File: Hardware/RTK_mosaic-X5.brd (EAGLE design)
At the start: 151.8 x 101.6 mm, 370 parts, among them J2 MAGJACK-POE, J3 MICRO-SD-PUSH-PUSH-EXT-PIN, J4 Vertical Qwiic Connector, J9 MAGJACK-POE, U1 ESP32-WROVER-IE, U10 POE_PSU-DP990X, U11 SN74AVC4T774PW, U17 URB2405YMD, U2 CH340C, U3 AP7361C-33FGEUDFN-8, U4 TXS0108, U5 TXS0108, U6 AP7361C-33FGEUDFN-8, U7 KSZ8041NL, U8 MOSAIC-X5X5, U9 KSZ8041NL

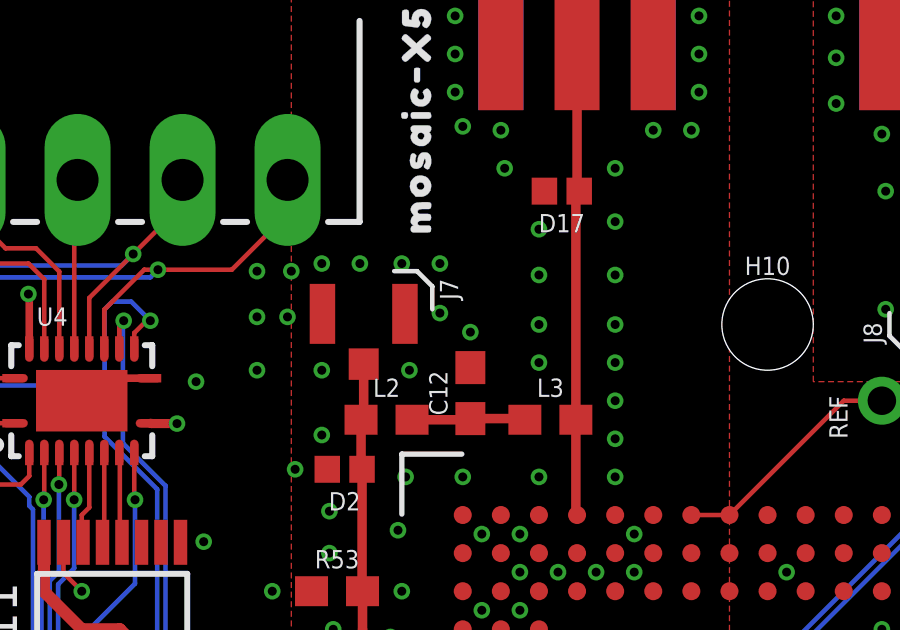
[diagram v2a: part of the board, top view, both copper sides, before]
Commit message: Adding u.FL connector for mosaic-H - with standoff holes for a u.FL-SMA daughter board
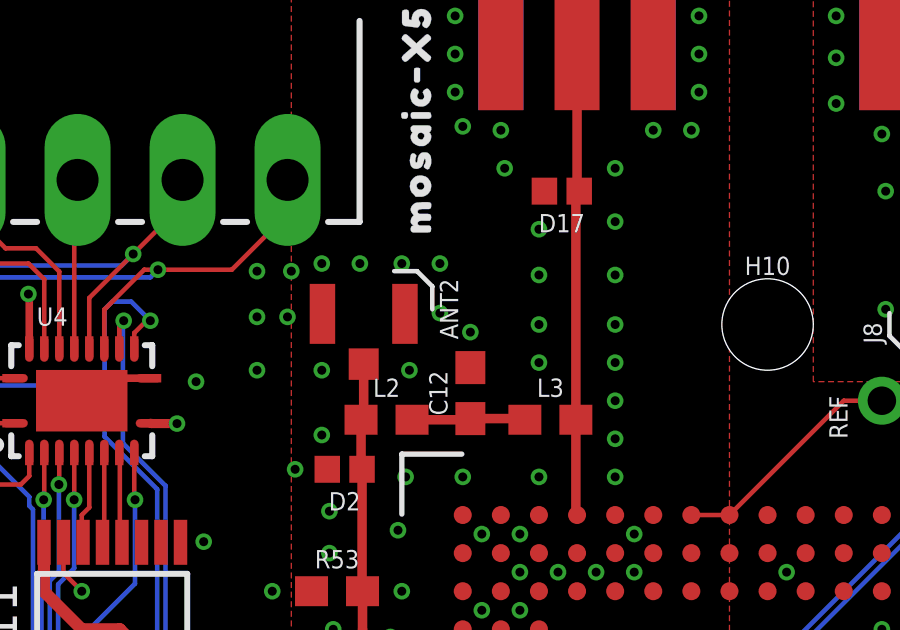
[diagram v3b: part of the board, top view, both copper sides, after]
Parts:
- removed J7: (no value), SparkFun-Connectors:U.FL_REDUCED_FOOTPRINT
- added ANT2: DNP, SparkFun-Connectors:U.FL_REDUCED_FOOTPRINT__NO_CREAM
- renumbered MOSAIC_RF to ANT1
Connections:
- net N$6 renamed VANT
- net ANT2: now also ANT2.FEED; no longer J7.FEED
- net GND: now also ANT2.1, ANT2.2; no longer J7.1, J7.2
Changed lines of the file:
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@@
 <drawing>
 <settings>
-<setting alwaysvectorfont="no"/>
+<setting alwaysvectorfont="yes"/>
 <setting verticaltext="up"/>
 </settings>
@@
 <layers>
 <layer number="1" name="Top" color="4" fill="1" visible="yes" active="yes"/>
-<layer number="2" name="Route2" color="63" fill="1" visible="yes" active="yes"/>
-<layer number="15" name="Route15" color="23" fill="1" visible="yes" active="yes"/>
+<layer number="2" name="Route2" color="63" fill="1" visible="no" active="yes"/>
+<layer number="15" name="Route15" color="23" fill="1" visible="no" active="yes"/>
 <layer number="16" name="Bottom" color="1" fill="1" visible="yes" active="yes"/>
 <layer number="17" name="Pads" color="2" fill="1" visible="yes" active="yes"/>
@@
 <layer number="23" name="tOrigins" color="15" fill="1" visible="yes" active="yes"/>
 <layer number="24" name="bOrigins" color="15" fill="1" visible="yes" active="yes"/>
-<layer number="25" name="tNames" color="7" fill="1" visible="yes" active="yes"/>
-<layer number="26" name="bNames" color="7" fill="1" visible="yes" active="yes"/>
-<layer number="27" name="tValues" color="7" fill="1" visible="yes" active="yes"/>
-<layer number="28" name="bValues" color="7" fill="1" visible="yes" active="yes"/>
-<layer number="29" name="tStop" color="7" fill="3" visible="yes" active="yes"/>
-<layer number="30" name="bStop" color="7" fill="6" visible="yes" active="yes"/>
-<layer number="31" name="tCream" color="7" fill="4" visible="yes" active="yes"/>
-<layer number="32" name="bCream" color="7" fill="5" visible="yes" active="yes"/>
-<layer number="33" name="tFinish" color="6" fill="3" visible="yes" active="yes"/>
-<layer number="34" name="bFinish" color="6" fill="6" visible="yes" active="yes"/>
-<layer number="35" name="tGlue" color="7" fill="4" visible="yes" active="yes"/>
-<layer number="36" name="bGlue" color="7" fill="5" visible="yes" active="yes"/>
-<layer number="37" name="tTest" color="7" fill="1" visible="yes" active="yes"/>
-<layer number="38" name="bTest" color="7" fill="1" visible="yes" active="yes"/>
-<layer number="39" name="tKeepout" color="4" fill="11" visible="yes" active="yes"/>
-<layer number="40" name="bKeepout" color="1" fill="11" visible="yes" active="yes"/>
-<layer number="41" name="tRestrict" color="4" fill="10" visible="yes" active="yes"/>
-<layer number="42" name="bRestrict" color="1" fill="10" visible="yes" active="yes"/>
-<layer number="43" name="vRestrict" color="2" fill="10" visible="yes" active="yes"/>
-<layer number="44" name="Drills" color="7" fill="1" visible="yes" active="yes"/>
+<layer number="25" name="tNames" color="7" fill="1" visible="no" active="yes"/>
+<layer number="26" name="bNames" color="7" fill="1" visible="no" active="yes"/>
+<layer number="27" name="tValues" color="7" fill="1" visible="no" active="yes"/>
+<layer number="28" name="bValues" color="7" fill="1" visible="no" active="yes"/>
+<layer number="29" name="tStop" color="7" fill="3" visible="no" active="yes"/>
+<layer number="30" name="bStop" color="7" fill="6" visible="no" active="yes"/>
+<layer number="31" name="tCream" color="7" fill="4" visible="no" active="yes"/>
+<layer number="32" name="bCream" color="7" fill="5" visible="no" active="yes"/>
+<layer number="33" name="tFinish" color="6" fill="3" visible="no" active="yes"/>
+<layer number="34" name="bFinish" color="6" fill="6" visible="no" active="yes"/>
+<layer number="35" name="tGlue" color="7" fill="4" visible="no" active="yes"/>
+<layer number="36" name="bGlue" color="7" fill="5" visible="no" active="yes"/>
+<layer number="37" name="tTest" color="7" fill="1" visible="no" active="yes"/>
+<layer number="38" name="bTest" color="7" fill="1" visible="no" active="yes"/>
+<layer number="39" name="tKeepout" color="4" fill="11" visible="no" active="yes"/>
+<layer number="40" name="bKeepout" color="1" fill="11" visible="no" active="yes"/>
+<layer number="41" name="tRestrict" color="4" fill="10" visible="no" active="yes"/>
+<layer number="42" name="bRestrict" color="1" fill="10" visible="no" active="yes"/>
+<layer number="43" name="vRestrict" color="2" fill="10" visible="no" active="yes"/>
+<layer number="44" name="Drills" color="7" fill="1" visible="no" active="yes"/>
 <layer number="45" name="Holes" color="7" fill="1" visible="yes" active="yes"/>
-<layer number="46" name="Milling" color="3" fill="1" visible="yes" active="yes"/>
-<layer number="47" name="Measures" color="7" fill="1" visible="yes" active="yes"/>
-<layer number="48" name="Document" color="7" fill="1" visible="yes" active="yes"/>
-<layer number="49" name="Reference" color="7" fill="1" visible="yes" active="yes"/>
-<layer number="50" name="dxf" color="7" fill="1" visible="yes" active="yes"/>
+<layer number="46" name="Milling" color="3" fill="1" visible="no" active="yes"/>
+<layer number="47" name="Measures" color="7" fill="1" visible="no" active="yes"/>
+<layer number="48" name="Document" color="7" fill="1" visible="no" active="yes"/>
+<layer number="49" name="Reference" color="7" fill="1" visible="no" active="yes"/>
+<layer number="50" name="dxf" color="7" fill="1" visible="no" active="yes"/>
 <layer number="51" name="tDocu" color="6" fill="1" visible="yes" active="yes"/>
-<layer number="52" name="bDocu" color="7" fill="1" visible="yes" active="yes"/>
+<layer number="52" name="bDocu" color="7" fill="1" visible="no" active="yes"/>
 <layer number="3" name="Route3" color="17" fill="1" visible="no" active="no"/>
 <layer number="4" name="Route4" color="18" fill="1" visible="no" active="no"/>
@@
 <attribute name="VALUE" x="43.18" y="88.265" size="0.6096" layer="27" font="vector" ratio="20" align="top-center"/>
 </element>
-<element name="MOSAIC_RF" library="SparkFun-RF" package="SMA-EDGE" value="ANTENNA-SMA-GROUNDEDEDGE_SMA" x="69.85" y="99.314" smashed="yes">
+<element name="ANT1" library="SparkFun-RF" package="SMA-EDGE" value="ANTENNA-SMA-GROUNDEDEDGE_SMA" x="69.85" y="99.314" smashed="yes">
 <attribute name="PROD_ID" value="CONN-08289" x="60.96" y="113.284" size="1.778" layer="27" ratio="15" display="off"/>
 </element>
@@
 <element name="U$122" library="output" package="#SPEED#0" value="" x="142.494" y="100.076" smashed="yes" rot="MR0"/>
 <element name="U$2" library="output" package="MOSAIC#X50" value="" x="64.516" y="97.028" smashed="yes" rot="R90"/>
-<element name="J7" library="SparkFun-Connectors" package="U.FL_REDUCED_FOOTPRINT" value="" x="62.738" y="90.424" smashed="yes" rot="R270">
+<element name="ANT2" library="SparkFun-Connectors" package="U.FL_REDUCED_FOOTPRINT__NO_CREAM" value="DNP" x="62.738" y="90.424" smashed="yes" rot="R270">
 <attribute name="NAME" x="65.278" y="91.694" size="0.6096" layer="25" font="vector" ratio="20" rot="R270"/>
-<attribute name="PROD_ID" value="CONN-09193" x="71.628" y="95.504" size="1.778" layer="27" ratio="15" rot="R270" display="off"/>
-<attribute name="VALUE" x="60.198" y="91.694" size="0.6096" layer="27" font="vector" ratio="20" rot="R270" align="top-left"/>
+<attribute name="VALUE" value="DNP" x="60.198" y="91.694" size="0.6096" layer="27" font="vector" ratio="20" rot="R270" align="top-left"/>
 </element>
 <element name="D2" library="SparkFun-DiscreteSemi" package="0402" value="PESD0402" x="62.103" y="85.344" smashed="yes" rot="R180">
@@
 <contactref element="R43" pad="1"/>
 <contactref element="R44" pad="1"/>
-<contactref element="MOSAIC_RF" pad="GND@1"/>
-<contactref element="MOSAIC_RF" pad="GND@2"/>
-<contactref element="MOSAIC_RF" pad="GND@0"/>
-<contactref element="MOSAIC_RF" pad="GND@3"/>
+<contactref element="ANT1" pad="GND@1"/>
+<contactref element="ANT1" pad="GND@2"/>
+<contactref element="ANT1" pad="GND@0"/>
+<contactref element="ANT1" pad="GND@3"/>
 <contactref element="D17" pad="2"/>
 <via x="33.401" y="73.66" extent="1-16" drill="0.3"/>
@@
 <via x="39.37" y="72.39" extent="1-16" drill="0.3"/>
 <via x="128.27" y="59.69" extent="1-16" drill="0.3"/>
-<contactref element="J7" pad="2"/>
-<contactref element="J7" pad="1"/>
+<contactref element="ANT2" pad="2"/>
+<contactref element="ANT2" pad="1"/>
 <contactref element="D2" pad="2"/>
 <contactref element="R53" pad="1"/>
@@
 <signal name="ANT1">
 <contactref element="U8" pad="AC20"/>
-<contactref element="MOSAIC_RF" pad="SIG"/>
+<contactref element="ANT1" pad="SIG"/>
 <contactref element="D17" pad="1"/>
 <wire x1="69.922" y1="94.615" x2="69.85" y2="94.687" width="0.3175" layer="1"/>
@@
 <wire x1="69.811" y1="94.504" x2="69.922" y2="94.615" width="0.3175" layer="1" curve="-90"/>
 </signal>
-<signal name="N$6">
+<signal name="VANT">
 <contactref element="FB3" pad="2"/>
 <contactref element="U8" pad="P23"/>
@@
 <signal name="ANT2">
 <contactref element="U8" pad="V23"/>
-<contactref element="J7" pad="FEED"/>
+<contactref element="ANT2" pad="FEED"/>
 <contactref element="D2" pad="1"/>
 <contactref element="L2" pad="1"/>

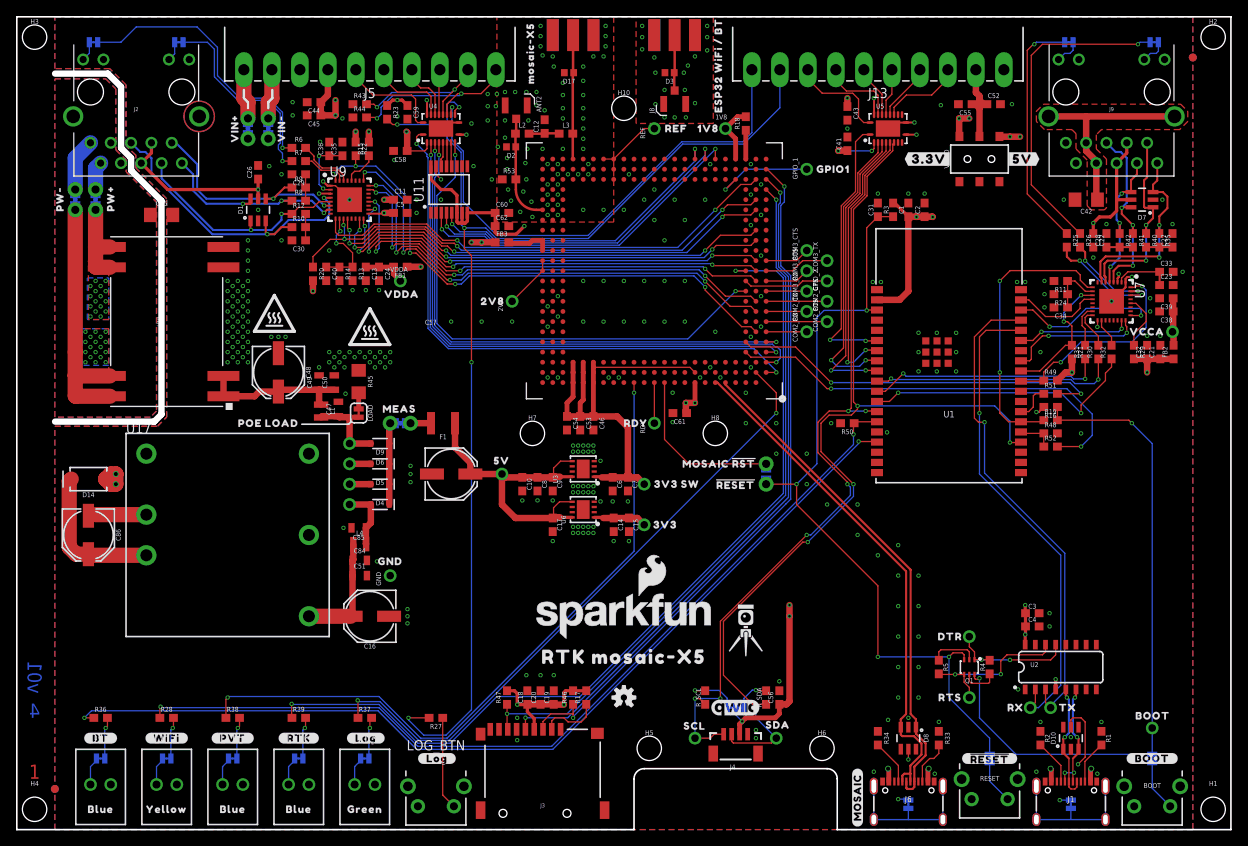
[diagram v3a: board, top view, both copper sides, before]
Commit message: Add Phy PROD_ID. Ready for manufacture
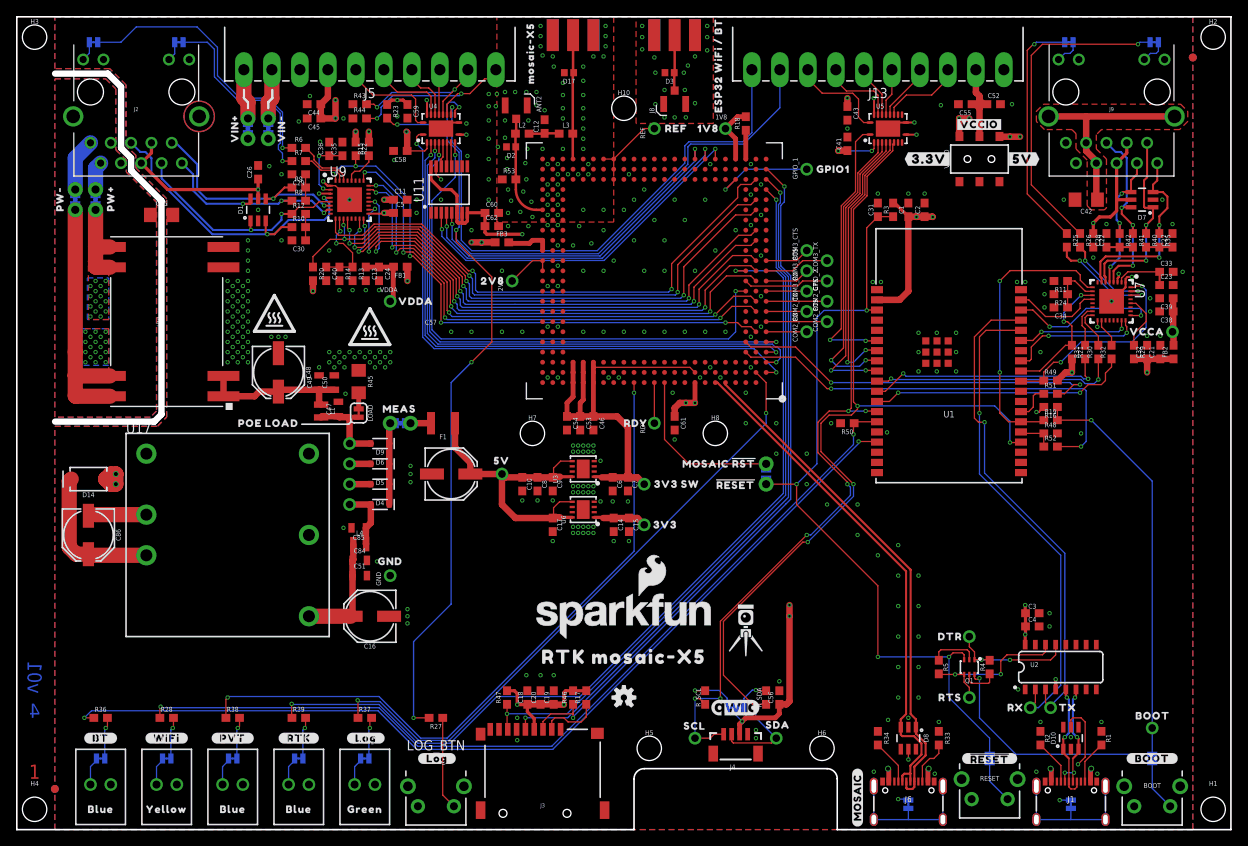
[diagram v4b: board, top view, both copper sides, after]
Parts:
- added U$100: (no value), output:#VCCIO#1
- U7, U9: value KSZ8041NL -> KSZ8041NLI
- moved VDDA 2.84 mm to (47.0, 66.0)
- moved 2V8 2.54 mm to (62.2, 68.6)
- moved U$41 2.54 mm to (62.0, 68.6)
- moved U$42 2.54 mm to (57.4, 68.6)
- moved U$97 1.99 mm to (53.1, 66.0)
- moved U$98 1.99 mm to (47.2, 66.0)
- moved C61 1.42 mm to (82.5, 50.8), turned to 270 degrees
- moved C60 1.27 mm to (59.7, 77.1)
- moved C62 1.27 mm to (59.7, 75.4)
- moved C45 0.38 mm to (37.5, 88.9)
- moved C44 0.25 mm to (37.5, 90.7)
- moved C59 0.13 mm to (49.1, 89.8)
- moved R23 0.13 mm to (46.6, 89.8)
- moved R44 0.13 mm to (43.2, 88.9)
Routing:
- net ETHER_CLK: track 59.7 -> 68.1 mm
- net ETHER_MDC: track 58.1 -> 66.2 mm
- net ETHER_MDIO: track 64.7 -> 72.4 mm
- net ETHER_CRSDV: track 57.5 -> 65.1 mm
- net ETHER_RXD0: track 57.0 -> 64.4 mm
- net ETHER_RXER: track 57.6 -> 65.0 mm
- net ETHER_RXD1: track 57.3 -> 64.4 mm
- net ETHER_TXEN: track 57.5 -> 64.1 mm
- net VCCIO: track 135.1 -> 141.0 mm
- net MOSAIC_PPSO_IO: track 64.3 -> 70.2 mm
- net MOSAIC_LOG_BTN: track 65.4 -> 69.7 mm
- net ETHER_TXD0: track 59.5 -> 63.1 mm
- net ETHER_TXD1: track 62.2 -> 65.0 mm
- net !BOOT!: track 83.2 -> 80.4 mm
- net ESP27_CRSDV: track 35.4 -> 32.7 mm
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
